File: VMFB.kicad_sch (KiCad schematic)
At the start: 121 parts, among them J1 Barrel_Jack_Switch, J10 Conn_01x03_Pin, J11 Conn_01x06_Pin, J12 Conn_01x06_Pin, J14 Conn_01x03_Pin, J15 Conn_01x03_Pin, J17 Conn_01x03_Pin, J18 Conn_01x02_Pin, J2 USB_B, J3 Screw_Terminal_01x02, J4 Screw_Terminal_01x03, J5 Conn_01x03_Pin, J6 Conn_01x03_Pin, J7 Conn_01x03_Pin, J9 Conn_01x02_Pin, Q1 BC547, Q2 BC547, Q3 BC547, Q4 BD139, Q5 TIP41C, Q6 BC547, Q7 BC547, U1 LM358, U2 NE555P, U3 NE555P, U4 NE555P, U5 NE555P

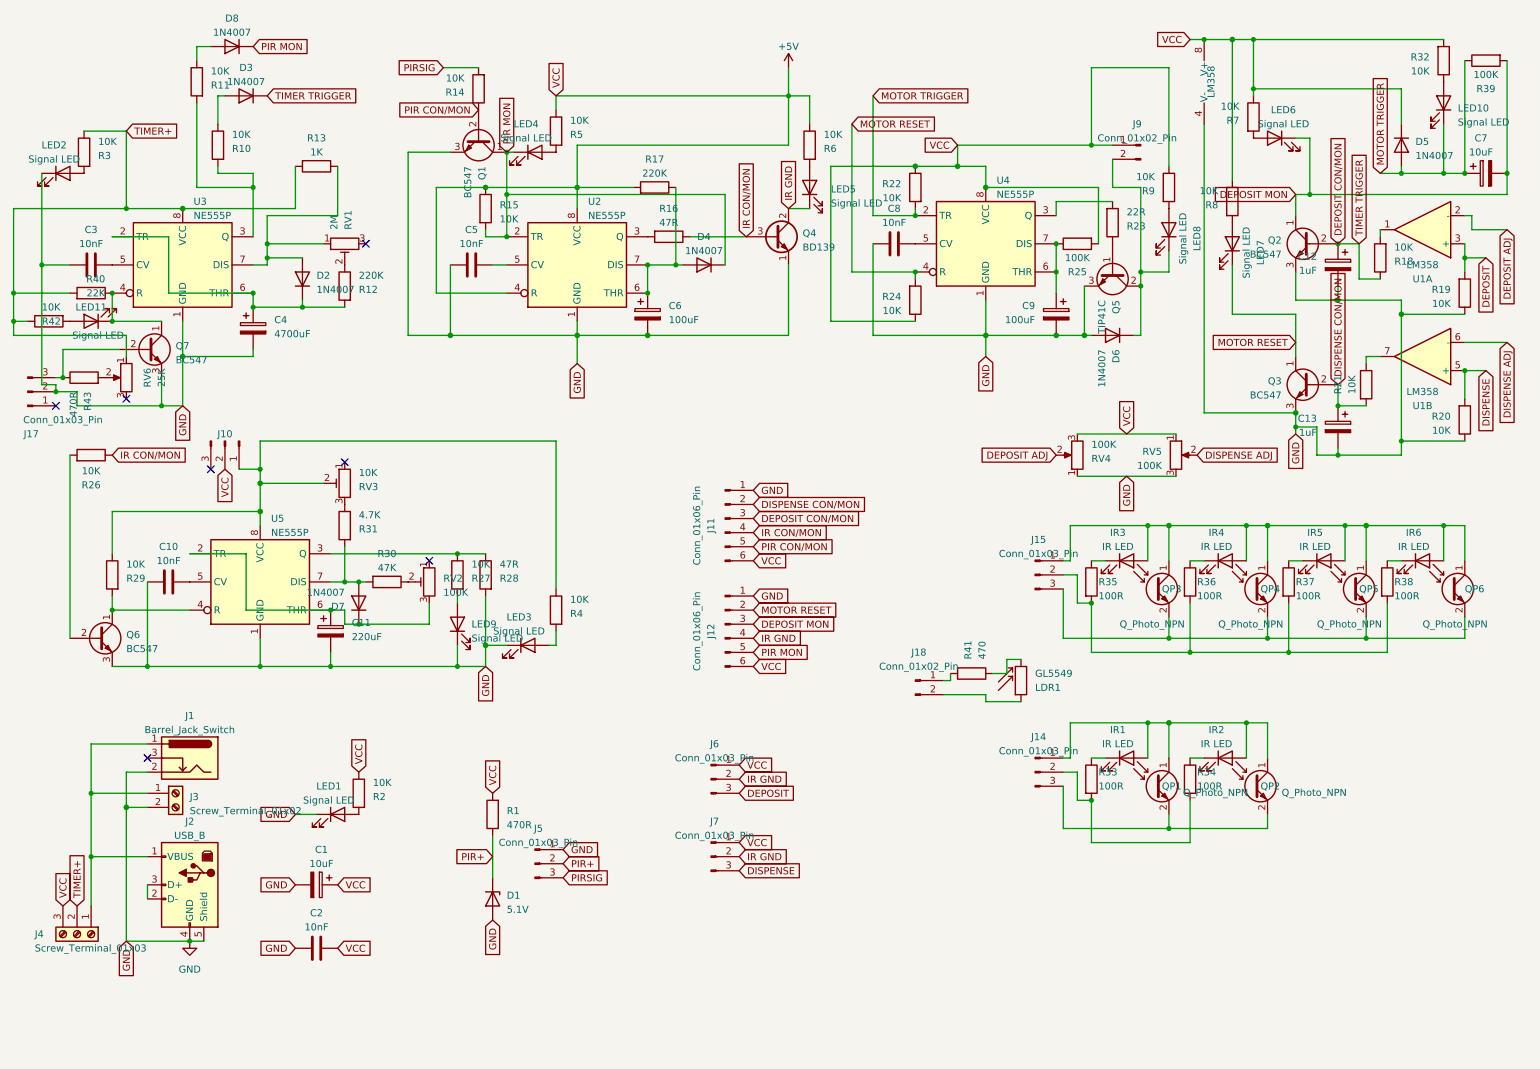
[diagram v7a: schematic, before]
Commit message: more adjustments to the daytimer and cleaned up schematic a bit
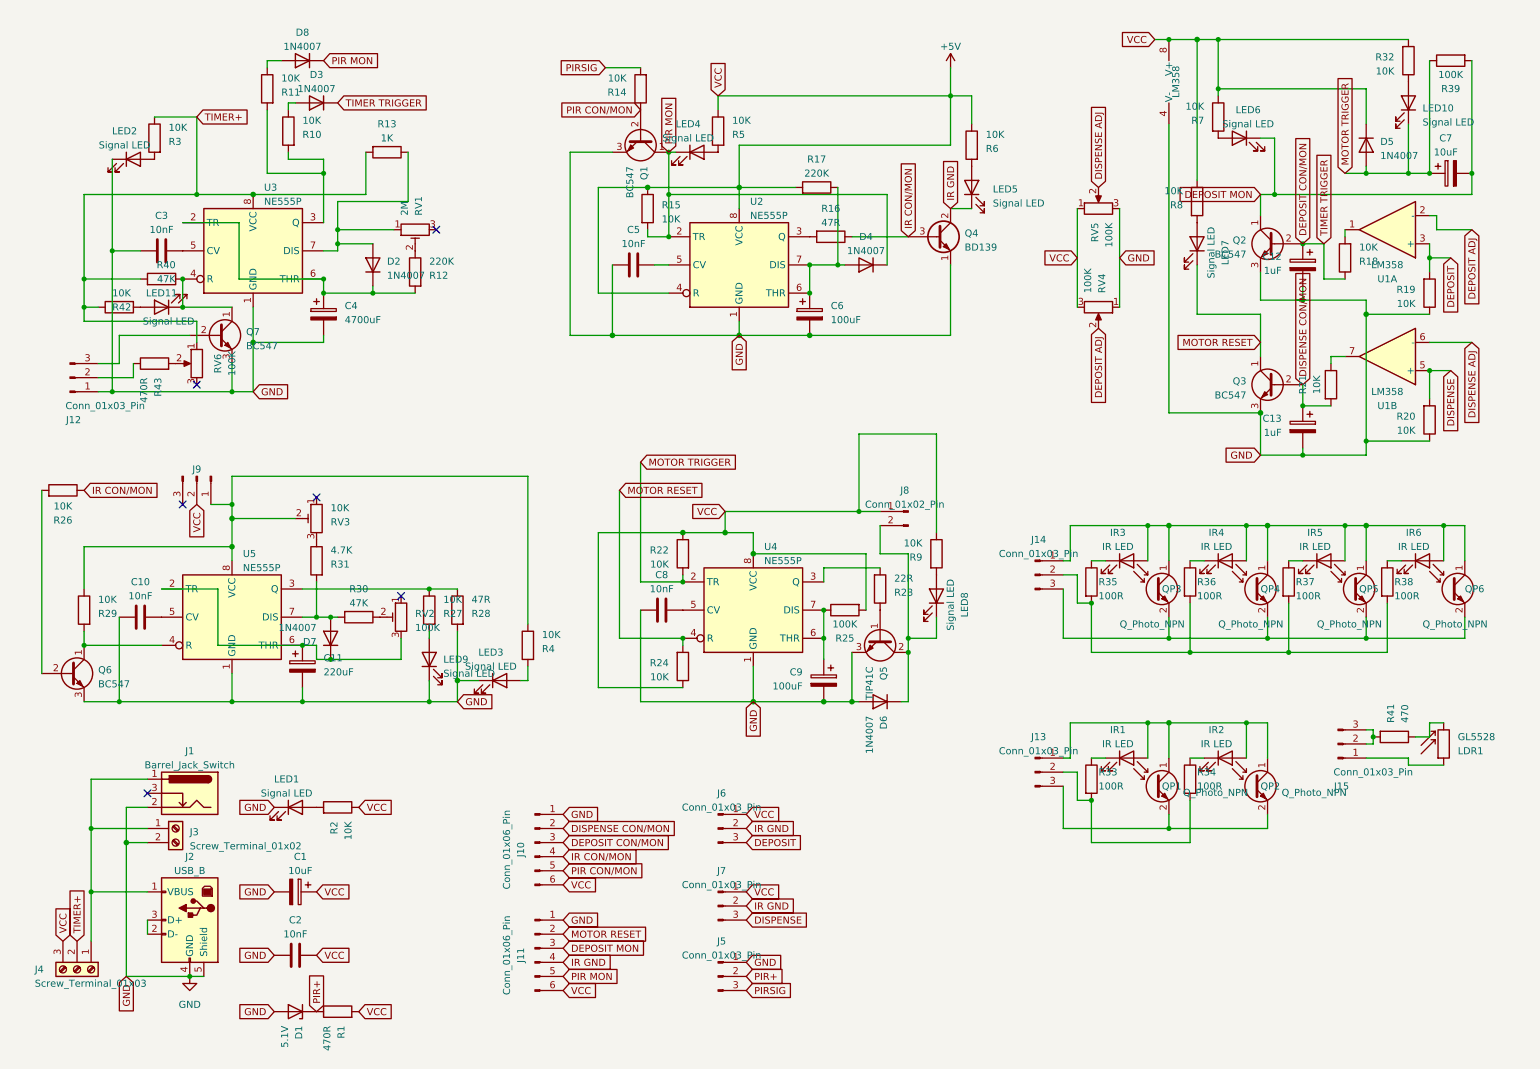
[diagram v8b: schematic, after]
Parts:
- removed J18: Conn_01x02_Pin, Connector_PinHeader_2.54mm:PinHeader_1x02_P2.54mm_Vertical, symbol Connector:Conn_01x02_Pin
- added J15: Conn_01x03_Pin, Connector_PinHeader_2.54mm:PinHeader_1x03_P2.54mm_Vertical, symbol Connector:Conn_01x03_Pin
- LDR1: value GL5549 -> GL5528
- R40: value 22K -> 47K
- RV6: value 25K -> 100K
- renumbered J11 to J10, J12 to J11, J17 to J12, J14 to J13, J15 to J14, J9 to J8, J10 to J9
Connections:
- net GND: now also J12.1 (Pin_1); no longer J12.2 (Pin_2)
- net at R41.2: now also J15.2 (Pin_2), J15.3 (Pin_3)
- net at J12.3 (Pin_3), Q7.2 (B): no longer R43.1
- net at LDR1.1: now also J15.1 (Pin_1)
- new net: J12.2 (Pin_2), R43.1
- no-connect marks 7 -> 6
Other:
- moved on the sheet: C1, C10, C11, C12, C13, C2, C3, C4, C5, C6, C7, C8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
